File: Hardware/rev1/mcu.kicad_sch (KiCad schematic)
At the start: 22 parts, among them J4 Conn_01x18_Socket, J5 Conn_01x18_Socket, Q1 AO3400A, SW1 SW_Push, U4 STM32F103C8Tx, Y1 16MHz

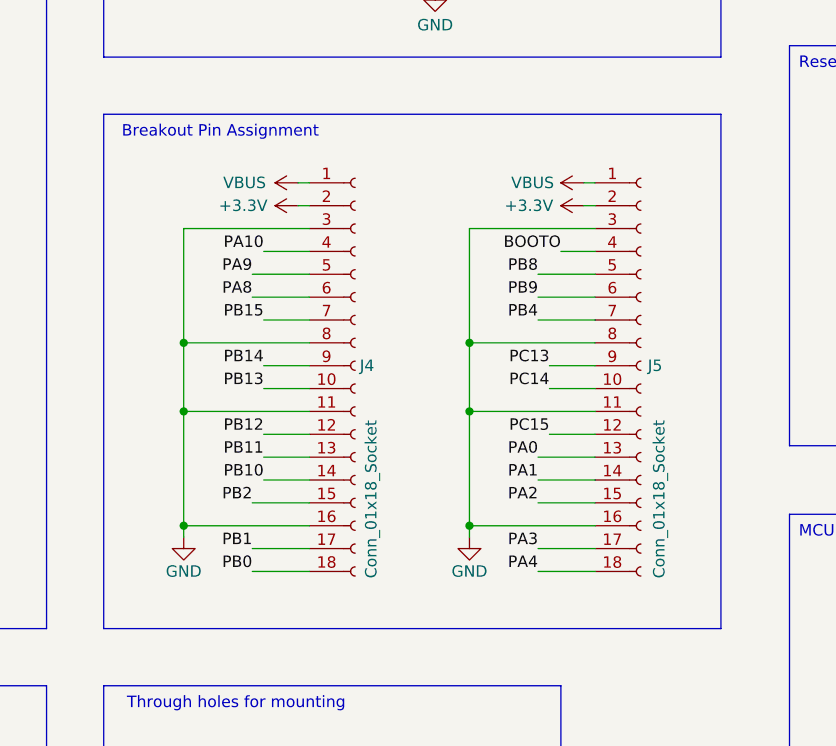
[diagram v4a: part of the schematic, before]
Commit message: Discarded a bunch of headers, finished traces, need stitching vias
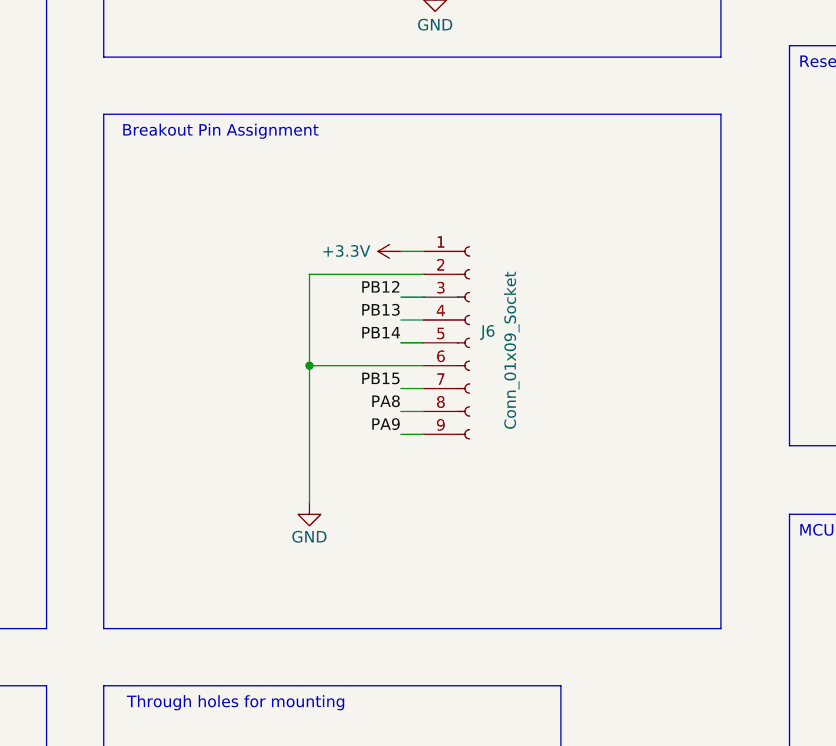
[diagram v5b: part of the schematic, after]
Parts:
- removed J4, J5: Conn_01x18_Socket, Connector_PinHeader_1.00mm:PinHeader_1x18_P1.00mm_Vertical, symbol Connector:Conn_01x18_Socket
- added J6: Conn_01x09_Socket, Connector_PinHeader_1.00mm:PinHeader_1x09_P1.00mm_Vertical, symbol Connector:Conn_01x09_Socket
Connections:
- net +3.3V: now also J6.1 (Pin_1)
- net GND: now also J6.2 (Pin_2), J6.6 (Pin_6)
- net PA8: now also J6.8 (Pin_8)
- net PA9: now also J6.9 (Pin_9)
- net PB12: now also J6.3 (Pin_3)
- net PB13: now also J6.4 (Pin_4)
- net PB14: now also J6.5 (Pin_5)
- net PB15: now also J6.7 (Pin_7)

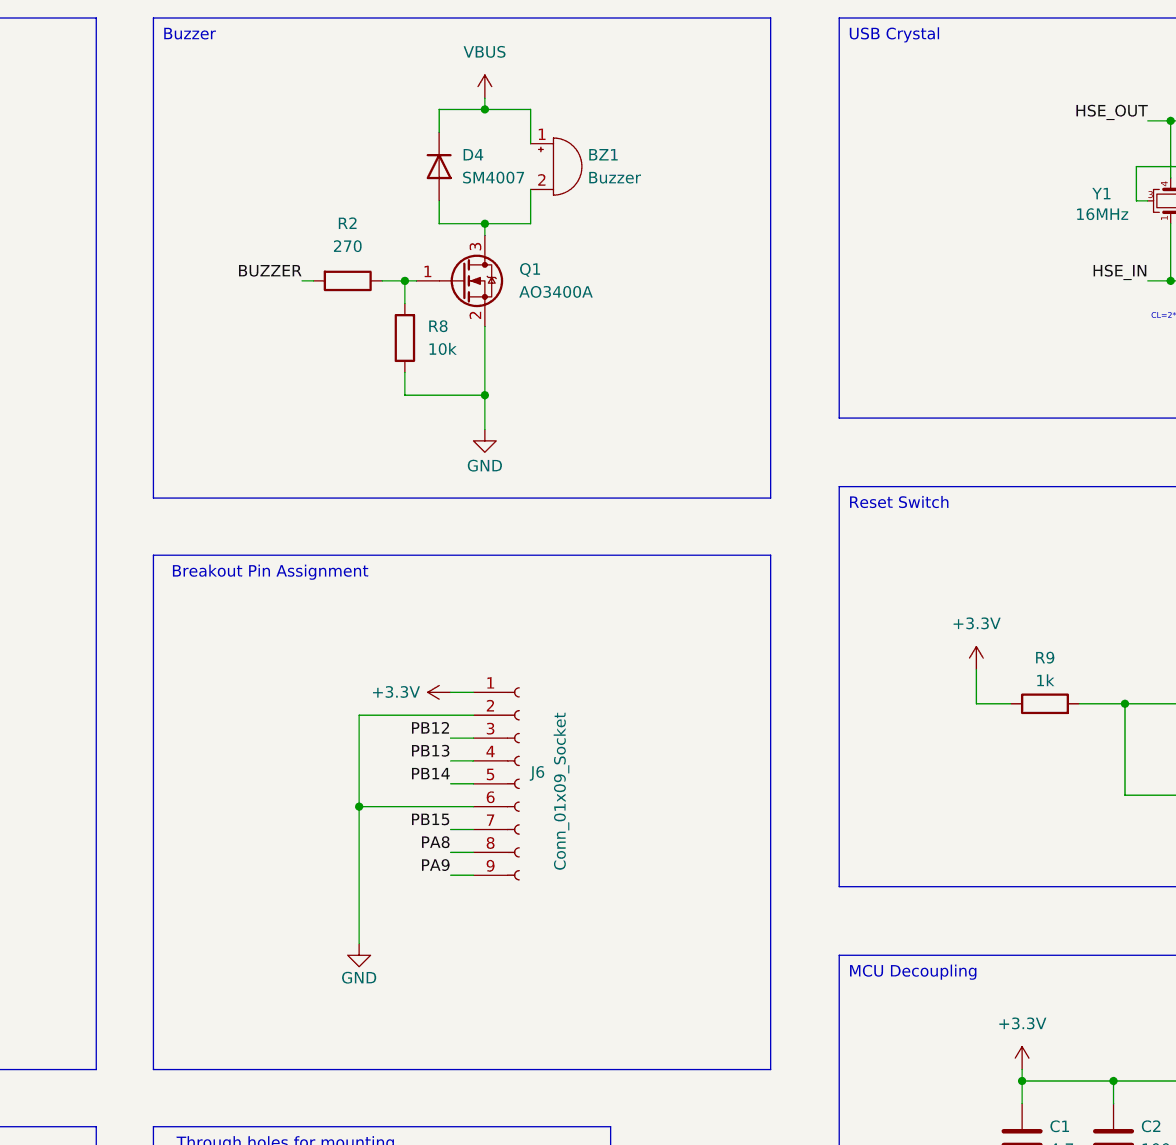
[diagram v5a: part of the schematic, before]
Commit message: Updated traces, moved mounting hole, selected switching diodes for power regulation
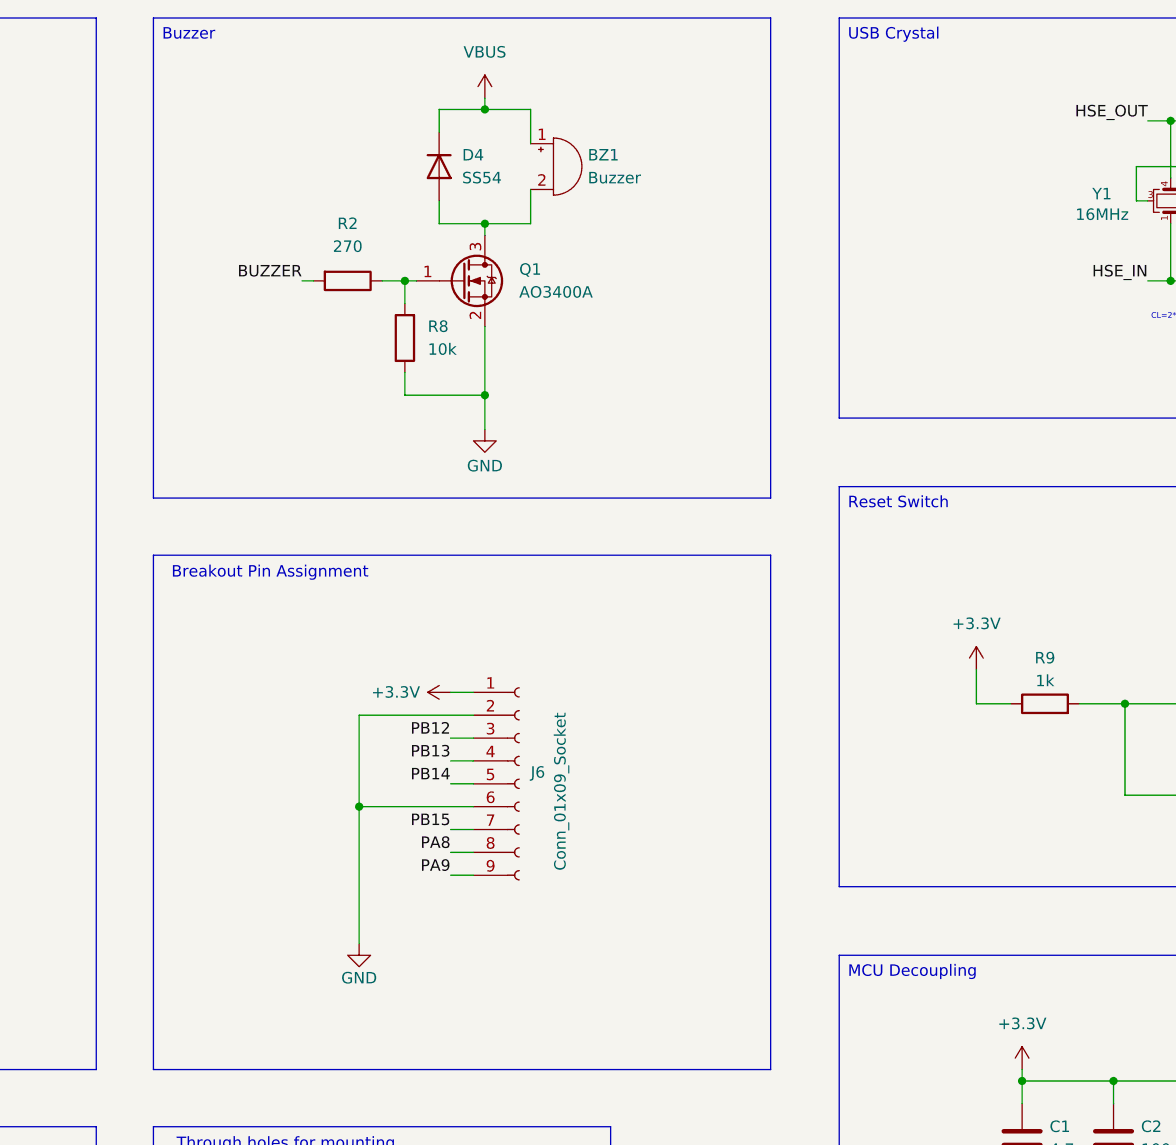
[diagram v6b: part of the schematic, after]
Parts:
- removed D4: SM4007, Diode_SMD:D_SOD-123F, symbol Diode:SM4007
- added D4: SS54, Diode_SMD:D_SMA, symbol Device:D
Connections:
- net VBUS: now also D4.1 (K)
- net at BZ1.2 (-), Q1.3 (D): now also D4.2 (A)
